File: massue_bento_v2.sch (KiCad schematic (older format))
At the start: 26 parts, among them K1 CONN_3, K2 CONN_3, K3 CONN_3, P1 TST, P2 TST, P3 SWD_CONN, P4 CONN_4, P5 TST, P6 TST, P7 TST, P8 TST, U1 LPC11U3x, U2 M25P40, X1 12.000 MHz

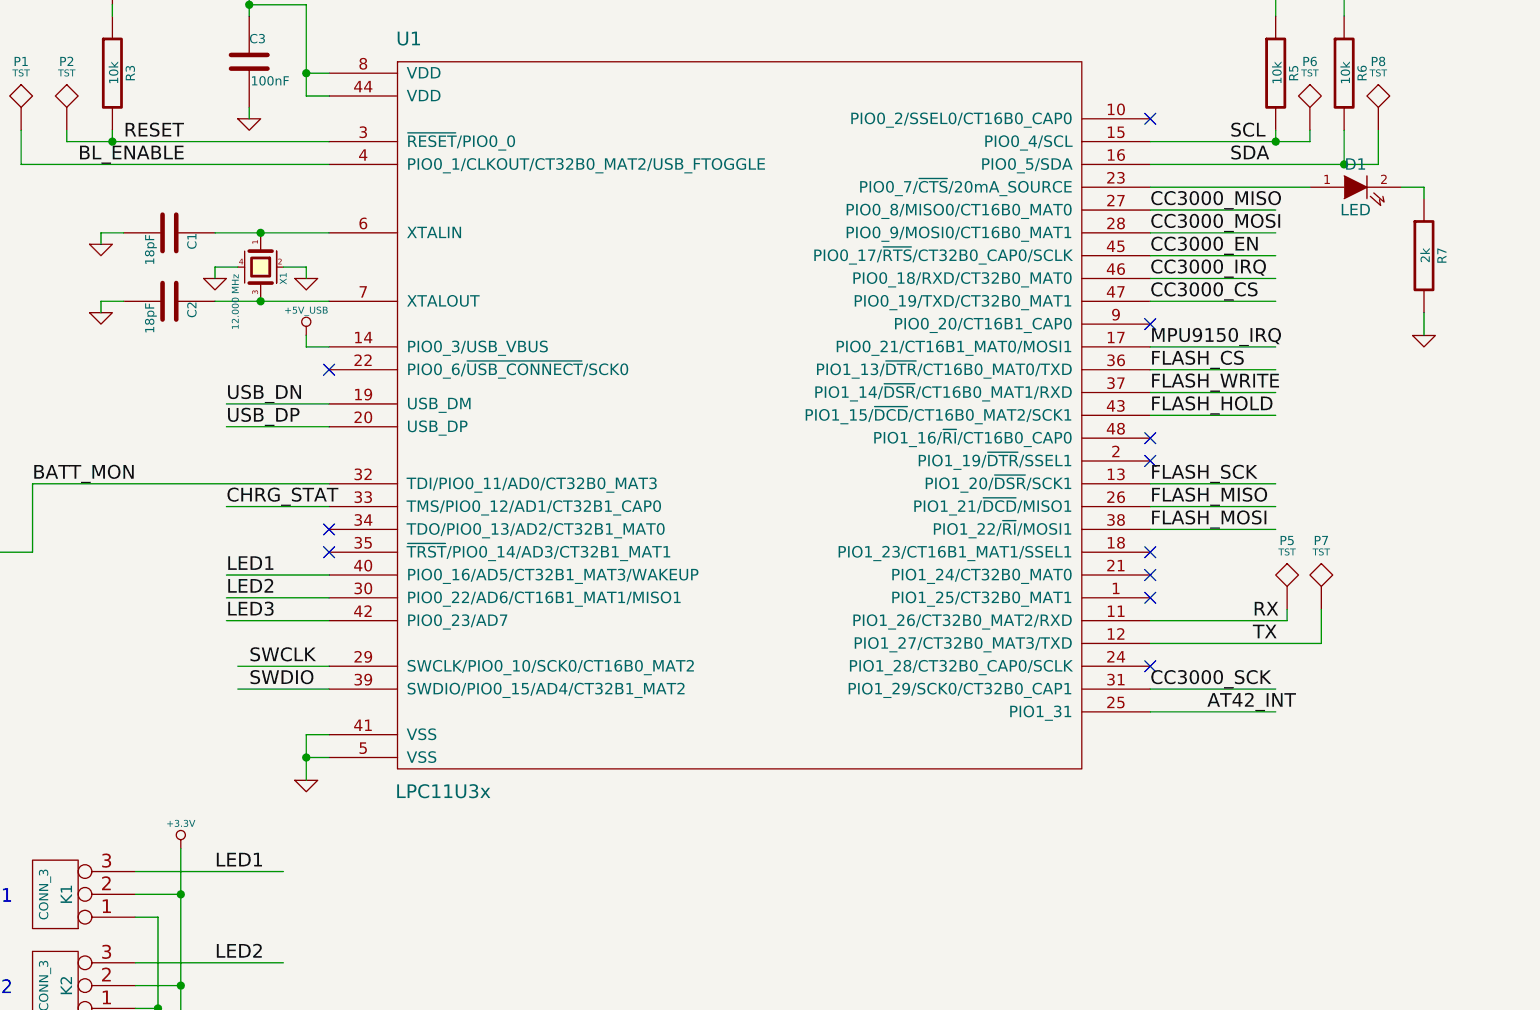
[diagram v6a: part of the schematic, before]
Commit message: Fix: LED strips are powered by VBAT and not 3.3V ; changed MCU pins to reflect component placement
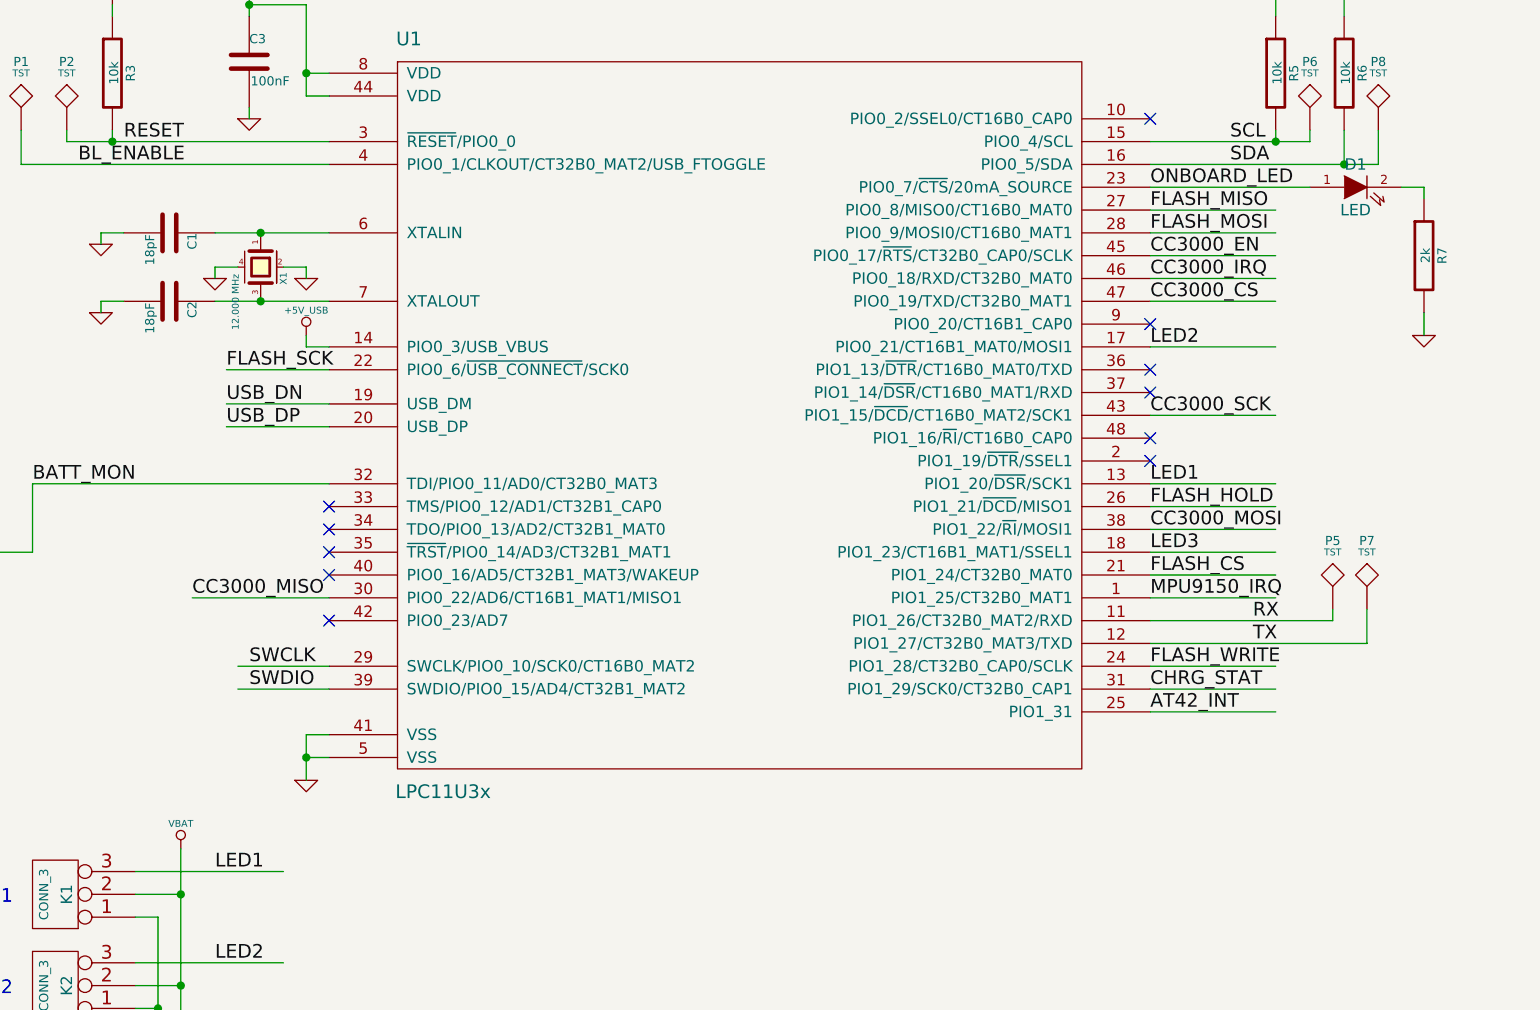
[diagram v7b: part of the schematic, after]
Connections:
- net labels added: ONBOARD_LED
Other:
- moved on the sheet: P5, P7
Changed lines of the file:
@@
-$EndSheet
-$Sheet
-S 9300 2950 1350 800
-U 53A572BF
-F0 "RF" 50
-F1 "massue_bento_v2_rf.sch" 50
-F2 "CC3000_SPI_CLK" I L 9300 3450 60
-F3 "CC3000_SPI_DIN" I L 9300 3550 60
-F4 "CC3000_SPI_IRQ" O L 9300 3200 60
-F5 "CC3000_SPI_DOUT" O L 9300 3650 60
-F6 "CC3000_SPI_CS" I L 9300 3350 60
-F7 "CC3000_SW_EN" I L 9300 3050 60
 $EndSheet
 $Sheet
@@
 	6250 1950 6950 1950
 Wire Wire Line
-	6250 3950 7000 3950
-Wire Wire Line
-	6250 3850 6850 3850
-Wire Wire Line
-	6850 3850 6850 3800
-Wire Wire Line
-	7000 3950 7000 3800
+	6250 3950 7200 3950
+Wire Wire Line
+	6250 3850 7050 3850
+Wire Wire Line
+	7200 3950 7200 3800
 Text Label 6700 3950 0    60   ~ 0
 TX
@@
 L TST P7
 U 1 1 53A6533B
-P 7000 3800
-F 0 "P7" H 7000 4100 40  0000 C CNN
-F 1 "TST" H 7000 4050 30  0000 C CNN
-F 2 "" H 7000 3800 60  0000 C CNN
-F 3 "" H 7000 3800 60  0000 C CNN
-	1    7000 3800
+P 7200 3800
+F 0 "P7" H 7200 4100 40  0000 C CNN
+F 1 "TST" H 7200 4050 30  0000 C CNN
+F 2 "" H 7200 3800 60  0000 C CNN
+F 3 "" H 7200 3800 60  0000 C CNN
+	1    7200 3800
 	1    0    0    -1
 $EndComp
@@
 L TST P5
 U 1 1 53A652B6
-P 6850 3800
-F 0 "P5" H 6850 4100 40  0000 C CNN
-F 1 "TST" H 6850 4050 30  0000 C CNN
-F 2 "" H 6850 3800 60  0000 C CNN
-F 3 "" H 6850 3800 60  0000 C CNN
-	1    6850 3800
+P 7050 3800
+F 0 "P5" H 7050 4100 40  0000 C CNN
+F 1 "TST" H 7050 4050 30  0000 C CNN
+F 2 "" H 7050 3800 60  0000 C CNN
+F 3 "" H 7050 3800 60  0000 C CNN
+	1    7050 3800
 	1    0    0    -1
 $EndComp
@@
 Wire Wire Line
 	6250 4150 6800 4150
+Text Label 2050 3750 0    60   ~ 0
+CC3000_MISO
+Text Label 6250 3450 0    60   ~ 0
+CC3000_MOSI
+Text Label 6250 2950 0    60   ~ 0
+CC3000_SCK
+Wire Wire Line
+	6250 3250 6800 3250
+Wire Wire Line
+	6250 3350 6800 3350
+Wire Wire Line
+	6250 3450 6800 3450
+Text Label 2200 2750 0    60   ~ 0
+FLASH_SCK
 Text Label 6250 2050 0    60   ~ 0
-CC3000_MISO
+FLASH_MISO
 Text Label 6250 2150 0    60   ~ 0
-CC3000_MOSI
-Text Label 6250 4150 0    60   ~ 0
-CC3000_SCK
-Wire Wire Line
-	6250 3250 6800 3250
-Wire Wire Line
-	6250 3350 6800 3350
-Wire Wire Line
-	6250 3450 6800 3450
-Text Label 6250 3250 0    60   ~ 0
-FLASH_SCK
-Text Label 6250 3350 0    60   ~ 0
-FLASH_MISO
-Text Label 6250 3450 0    60   ~ 0
 FLASH_MOSI
 Wire Wire Line
@@
 CC3000_CS
 Wire Wire Line
-	6250 2750 6800 2750
-Wire Wire Line
-	6250 2850 6800 2850
-Wire Wire Line
 	6250 2950 6800 2950
-Text Label 6250 2750 0    60   ~ 0
+Text Label 6250 3650 0    60   ~ 0
 FLASH_CS
-Text Label 6250 2850 0    60   ~ 0
+Text Label 6250 4050 0    60   ~ 0
 FLASH_WRITE
-Text Label 6250 2950 0    60   ~ 0
+Text Label 6250 3350 0    60   ~ 0
 FLASH_HOLD
-Wire Wire Line
-	2200 3350 2650 3350
-Text Label 2200 3350 0    60   ~ 0
+Text Label 6250 4150 0    60   ~ 0
 CHRG_STAT
 $Comp
@@
 LED3
 $Comp
-L +3.3V #PWR023
-U 1 1 53A769C5
-P 2000 4850
-F 0 "#PWR023" H 2000 4810 30  0001 C CNN
-F 1 "+3.3V" H 2000 4960 30  0000 C CNN
-F 2 "" H 2000 4850 60  0000 C CNN
-F 3 "" H 2000 4850 60  0000 C CNN
-	1    2000 4850
-	1    0    0    -1
-$EndComp
-$Comp
-L GND #PWR024
+L GND #PWR023
 U 1 1 53A76E3F
 P 1900 6050
-F 0 "#PWR024" H 1900 6050 30  0001 C CNN
+F 0 "#PWR023" H 1900 6050 30  0001 C CNN
 F 1 "GND" H 1900 5980 30  0001 C CNN
 F 2 "" H 1900 6050 60  0000 C CNN
@@
 NB: LED data is handled by bit-banging (1 SPI port is used by the CC3000\nand the other by the flash memory)\nAny pin can be used for the LED data, 3 separate outputs increase code efficiency.
 Wire Wire Line
-	2200 3650 2650 3650
-Wire Wire Line
-	2200 3750 2650 3750
-Wire Wire Line
-	2200 3850 2650 3850
-Text Label 2200 3650 0    60   ~ 0
+	2050 3750 2650 3750
+Text Label 6250 3250 0    60   ~ 0
 LED1
-Text Label 2200 3750 0    60   ~ 0
+Text Label 6250 2650 0    60   ~ 0
 LED2
-Text Label 2200 3850 0    60   ~ 0
+Text Label 6250 3550 0    60   ~ 0
 LED3
-NoConn ~ 2650 2750
 NoConn ~ 2650 3450
 NoConn ~ 2650 3550
-NoConn ~ 6250 4050
-NoConn ~ 6250 3750
-NoConn ~ 6250 3650
-NoConn ~ 6250 3550
 NoConn ~ 6250 3050
 NoConn ~ 6250 2550
 NoConn ~ 6250 1650
 $Comp
-L PWR_FLAG #FLG025
+L PWR_FLAG #FLG024
 U 1 1 53A7B5D5
 P 950 7500
-F 0 "#FLG025" H 950 7595 30  0001 C CNN
+F 0 "#FLG024" H 950 7595 30  0001 C CNN
 F 1 "PWR_FLAG" H 950 7680 30  0000 C CNN
 F 2 "" H 950 7500 60  0000 C CNN
@@
 $EndComp
 $Comp
-L PWR_FLAG #FLG026
+L PWR_FLAG #FLG025
 U 1 1 53A7B6EC
 P 1350 7500
-F 0 "#FLG026" H 1350 7595 30  0001 C CNN
+F 0 "#FLG025" H 1350 7595 30  0001 C CNN
 F 1 "PWR_FLAG" H 1350 7680 30  0000 C CNN
 F 2 "" H 1350 7500 60  0000 C CNN
@@
 $EndComp
 $Comp
-L GND #PWR027
+L GND #PWR026
 U 1 1 53A7B6F9
 P 950 7600
-F 0 "#PWR027" H 950 7600 30  0001 C CNN
+F 0 "#PWR026" H 950 7600 30  0001 C CNN
 F 1 "GND" H 950 7530 30  0001 C CNN
 F 2 "" H 950 7600 60  0000 C CNN
@@
 	950  7600 950  7500
 $Comp
-L +5V_USB #PWR028
+L +5V_USB #PWR027
 U 1 1 53A7B810
 P 1550 7500
-F 0 "#PWR028" H 1550 7560 30  0001 C CNN
+F 0 "#PWR027" H 1550 7560 30  0001 C CNN
 F 1 "+5V_USB" H 1550 7610 30  0000 C CNN
 F 2 "" H 1550 7500 60  0000 C CNN
@@
 Wire Wire Line
 	6250 2650 6800 2650
-Text Label 6250 2650 0    60   ~ 0
+Text Label 6250 3750 0    60   ~ 0
 MPU9150_IRQ
 Wire Wire Line
@@
 Wire Wire Line
 	6250 4250 6800 4250
-Text Label 6500 4250 0    60   ~ 0
+Text Label 6250 4250 0    60   ~ 0
 AT42_INT
+Wire Wire Line
+	2650 2750 2200 2750
+Text Label 6250 1950 0    60   ~ 0
+ONBOARD_LED
+$Sheet
+S 9300 2950 1350 800
+U 53A572BF
+F0 "RF" 50
+F1 "massue_bento_v2_rf.sch" 50
+F2 "CC3000_SPI_CLK" I L 9300 3450 60
+F3 "CC3000_SPI_DIN" I L 9300 3550 60
+F4 "CC3000_SPI_IRQ" O L 9300 3200 60
+F5 "CC3000_SPI_DOUT" O L 9300 3650 60
+F6 "CC3000_SPI_CS" I L 9300 3350 60
+F7 "CC3000_SW_EN" I L 9300 3050 60
+$EndSheet
+Wire Wire Line
+	6250 3750 6800 3750
+Wire Wire Line
+	7050 3850 7050 3800
+$Comp
+L VBAT #PWR028
+U 1 1 53AF7479
+P 2000 4850
+F 0 "#PWR028" H 2000 4910 30  0001 C CNN
+F 1 "VBAT" H 2000 4960 30  0000 C CNN
+F 2 "" H 2000 4850 60  0000 C CNN
+F 3 "" H 2000 4850 60  0000 C CNN
+	1    2000 4850
+	1    0    0    -1
+$EndComp
+Wire Wire Line
+	6250 4050 6800 4050
+Wire Wire Line
+	6250 3650 6800 3650
+Wire Wire Line
+	6250 3550 6800 3550
+NoConn ~ 2650 3350
+NoConn ~ 2650 3650
+NoConn ~ 2650 3850
+NoConn ~ 6250 2750
+NoConn ~ 6250 2850
 $EndSCHEMATC

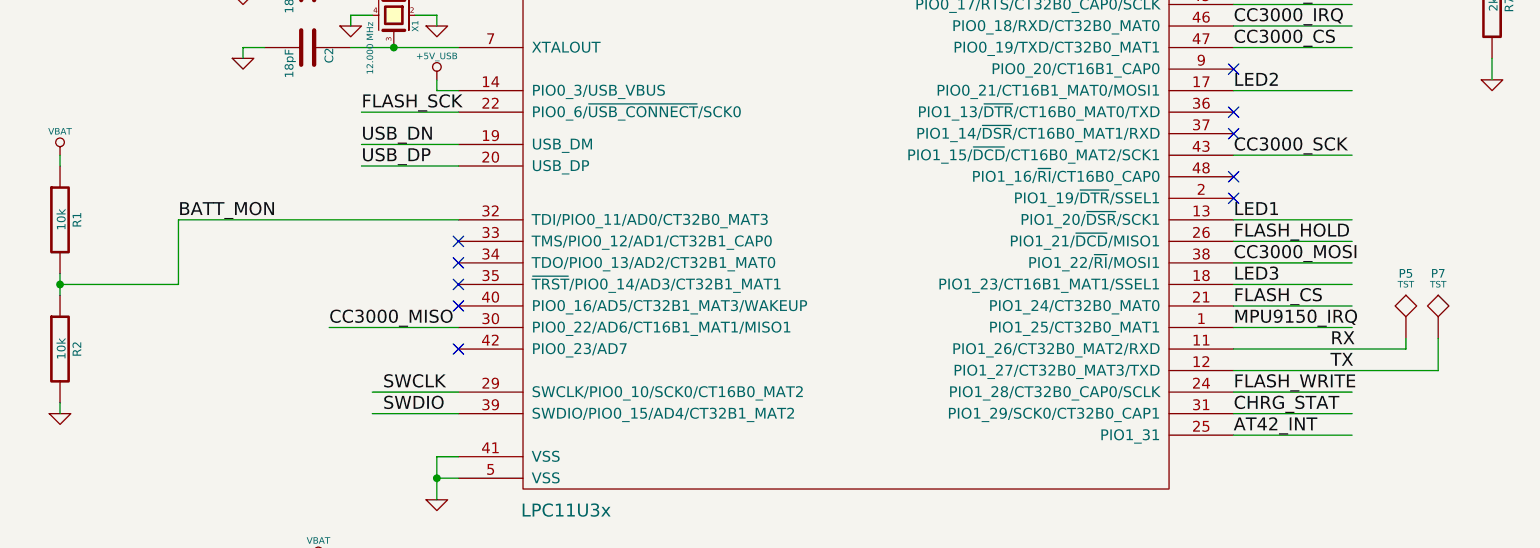
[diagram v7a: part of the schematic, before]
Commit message: New: first routing for almost all signals
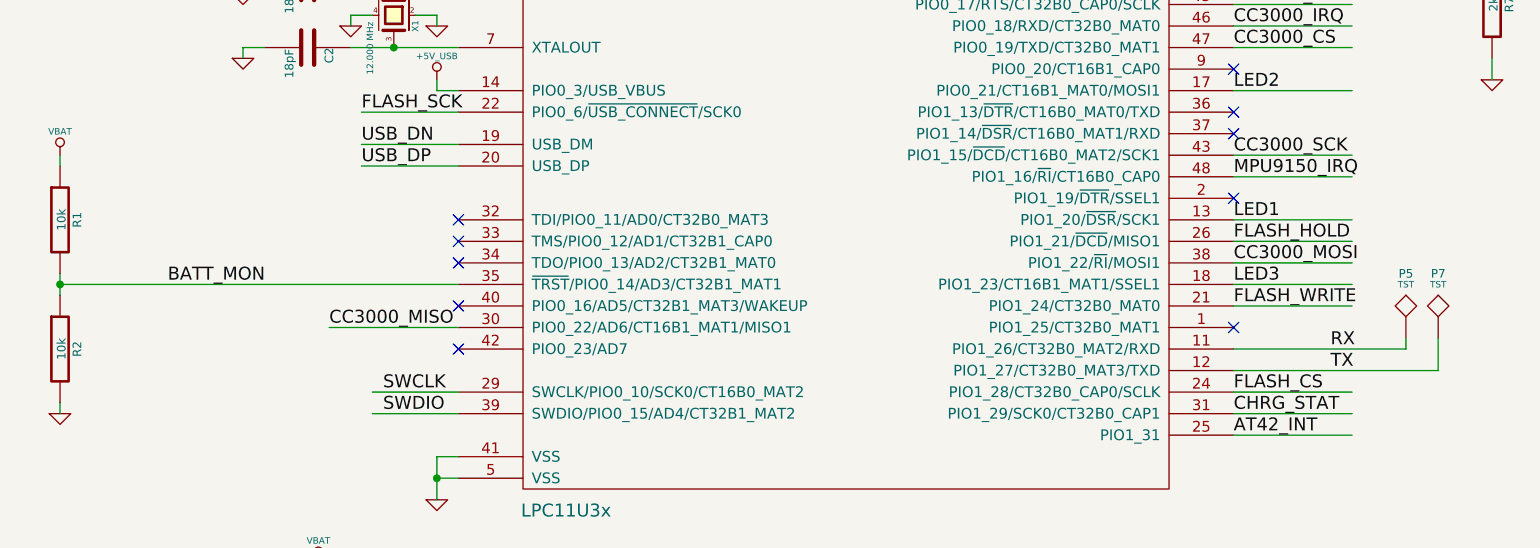
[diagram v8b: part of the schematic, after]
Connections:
- wire segments 125 -> 123
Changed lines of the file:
@@
 Wire Wire Line
 	6250 2950 6800 2950
+Text Label 6250 4050 0    60   ~ 0
+FLASH_CS
 Text Label 6250 3650 0    60   ~ 0
-FLASH_CS
-Text Label 6250 4050 0    60   ~ 0
 FLASH_WRITE
 Text Label 6250 3350 0    60   ~ 0
@@
 	800  3000 800  2950
 Wire Wire Line
-	800  3550 1350 3550
-Wire Wire Line
-	1350 3550 1350 3250
-Wire Wire Line
-	1350 3250 2650 3250
+	800  3550 2650 3550
 Connection ~ 800  3550
-Text Label 1350 3250 0    60   ~ 0
+Text Label 1300 3550 0    60   ~ 0
 BATT_MON
 $Comp
@@
 LED3
 NoConn ~ 2650 3450
-NoConn ~ 2650 3550
-NoConn ~ 6250 3050
+NoConn ~ 2650 3250
+NoConn ~ 6250 3750
 NoConn ~ 6250 2550
 NoConn ~ 6250 1650
@@
 Wire Wire Line
 	6250 2650 6800 2650
-Text Label 6250 3750 0    60   ~ 0
+Text Label 6250 3050 0    60   ~ 0
 MPU9150_IRQ
 Wire Wire Line
@@
 $EndSheet
 Wire Wire Line
-	6250 3750 6800 3750
-Wire Wire Line
 	7050 3850 7050 3800
 $Comp
@@
 NoConn ~ 6250 2750
 NoConn ~ 6250 2850
+Wire Wire Line
+	6250 3050 6800 3050
 $EndSCHEMATC
